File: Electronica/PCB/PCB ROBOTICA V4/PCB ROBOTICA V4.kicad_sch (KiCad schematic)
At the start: 13 parts, among them J1 Ultrasonico 1, J2 Screw_Terminal_01x02, J3 Ultrasonico 2, J4 Ultrasonico 3, J5 Conn_02x05_Counter_Clockwise, J6 Screw_Terminal_01x02

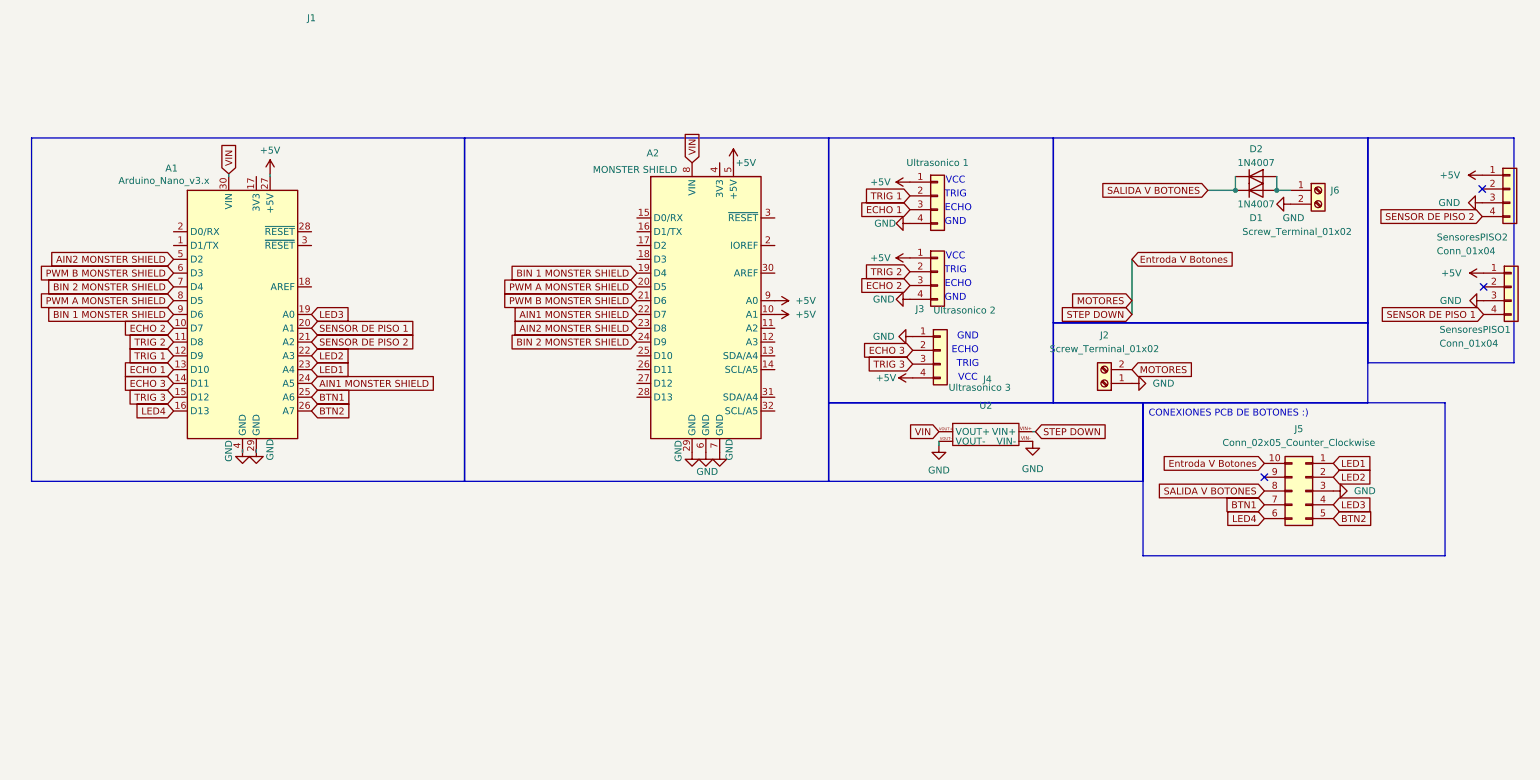
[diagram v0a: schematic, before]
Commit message: Esquematico PCB V4 terminado
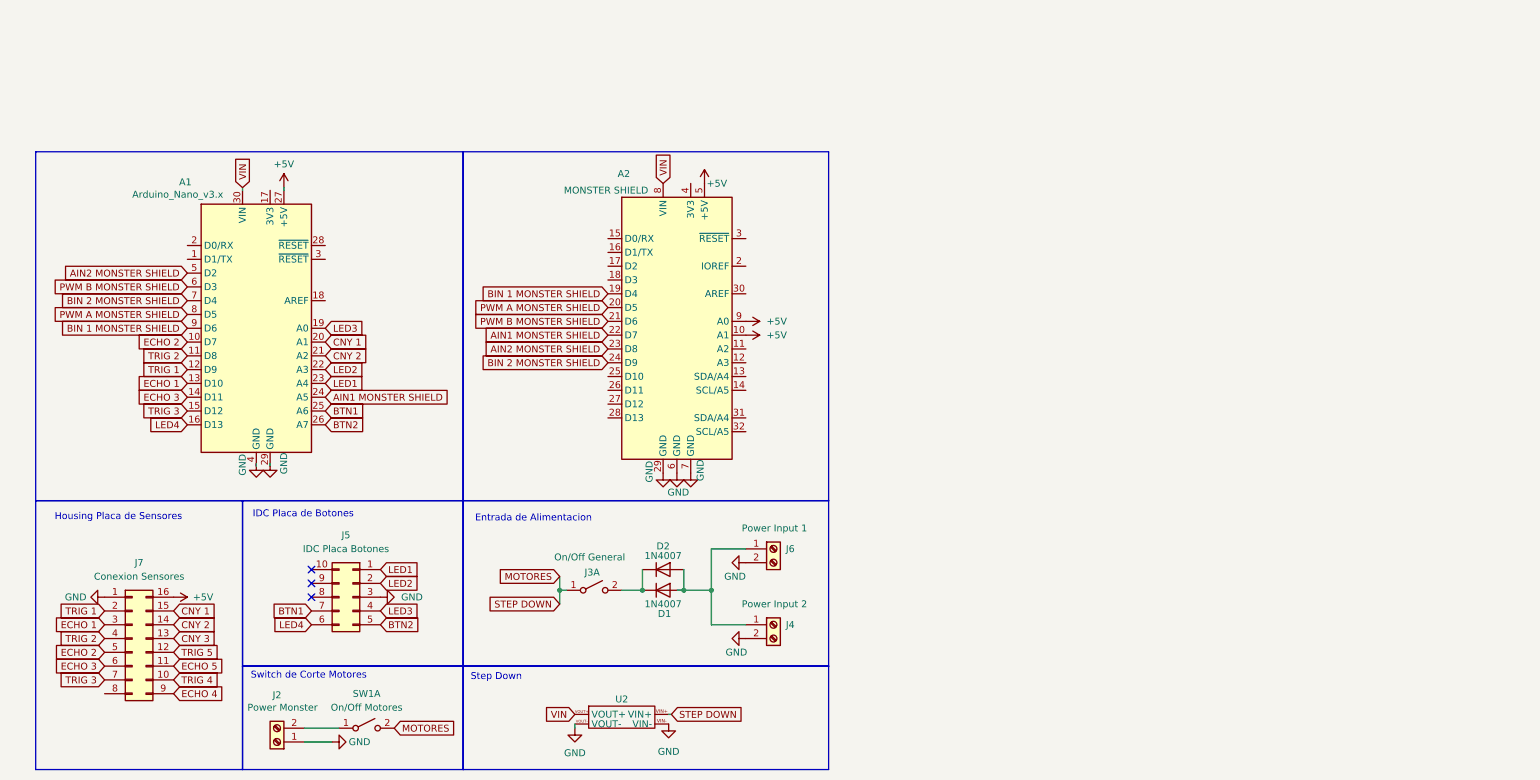
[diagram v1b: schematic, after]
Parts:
- removed J1: Ultrasonico 1, Connector_Molex:Molex_KK-254_AE-6410-04A_1x04_P2.54mm_Vertical, symbol Connector_Generic:Conn_01x04
- removed J3: Ultrasonico 2, Connector_Molex:Molex_KK-254_AE-6410-04A_1x04_P2.54mm_Vertical, symbol Connector_Generic:Conn_01x04
- removed J4: Ultrasonico 3, Connector_Molex:Molex_KK-254_AE-6410-04A_1x04_P2.54mm_Vertical, symbol Connector_Generic:Conn_01x04
- removed SensoresPISO1: Conn_01x04, Connector_Molex:Molex_KK-254_AE-6410-04A_1x04_P2.54mm_Vertical, symbol Connector_Generic:Conn_01x04
- removed SensoresPISO2: Conn_01x04, Connector_PinSocket_2.54mm:PinSocket_1x04_P2.54mm_Vertical, symbol Connector_Generic:Conn_01x04
- added J3: On/Off General, TerminalBlock:TerminalBlock_bornier-2_P5.08mm, symbol Switch:SW_DPST_x2
- added J4: Power Input 2, Connector_AMASS:AMASS_XT60-M_1x02_P7.20mm_Vertical, symbol Connector:Screw_Terminal_01x02
- added J7: Conexion Sensores, Connector_PinHeader_2.54mm:PinHeader_2x08_P2.54mm_Horizontal, symbol Connector_Generic:Conn_02x08_Counter_Clockwise
- added SW1: On/Off Motores, Button_Switch_THT:SW_Slide_SPDT_Angled_CK_OS102011MA1Q, symbol Switch:SW_DPST_x2
- J2: value Screw_Terminal_01x02 -> Power Monster
- J5: value Conn_02x05_Counter_Clockwise -> IDC Placa Botones
- J6: value Screw_Terminal_01x02 -> Power Input 1
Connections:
- net +5V: now also J7.16 (Pin_16)
- net ECHO 1: now also J7.3 (Pin_3)
- net ECHO 2: now also J7.5 (Pin_5)
- net ECHO 3: now also J7.6 (Pin_6)
- net GND: now also J4.2 (Pin_2), J7.1 (Pin_1)
- net TRIG 1: now also J7.2 (Pin_2)
- net TRIG 2: now also J7.4 (Pin_4)
- net TRIG 3: now also J7.7 (Pin_7)
- net at D1.2 (A), D2.2 (A), J6.1 (Pin_1): now also J4.1 (Pin_1)
- removed net Entroda V Botones: J2.2 (Pin_2), J5.10 (Pin_10), U2.VIN+
- net SALIDA V BOTONES: no longer names the net of D1.1 (K), D2.1 (K)
- net SALIDA V BOTONES: now also J3.2 (B); no longer J5.8 (Pin_8)
- net SENSOR DE PISO 1 renamed CNY 1
- net CNY 1: now also J7.15 (Pin_15)
- net SENSOR DE PISO 2 renamed CNY 2
- net CNY 2: now also J7.14 (Pin_14)
- new net: J2.2 (Pin_2), SW1.1 (A)
- new net CNY 3: J7.13 (Pin_13)
- new net ECHO 4: J7.9 (Pin_9)
- new net ECHO 5: J7.11 (Pin_11)
- new net MOTORES: J3.1 (A), SW1.2 (B), U2.VIN+
- new net TRIG 4: J7.10 (Pin_10)
- new net TRIG 5: J7.12 (Pin_12)
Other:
- note added: "Entrada de Alimentacion"
- note added: "Housing Placa de Sensores"
- note added: "IDC Placa de Botones"
- note added: "Step Down"
- note added: "Switch de Corte Motores"
- note removed: "ECHO"
- note removed: "GND"
- note removed: "TRIG"
- note removed: "VCC"
- moved on the sheet: A1, A2, D1, D2, J2, J5, J6, U2
